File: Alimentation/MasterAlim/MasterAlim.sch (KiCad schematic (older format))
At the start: 51 parts, among them J1 Ext-Con, J10 Interf-Reg1, J11 AU Logic, J12 Interf-Reg2, J13 Interf-Reg3, J14 Interf-Reg4, J2 5V, J3 Bat. IN, J5 Direct Out, J6 Reg 1, J7 Reg 2, J8 Reg 3, J9 Reg 4, U1 74LS33, U3 ACS712xLCTR-20A, U6 PTN78020W_EUK-7, U7 ACS712xLCTR-20A

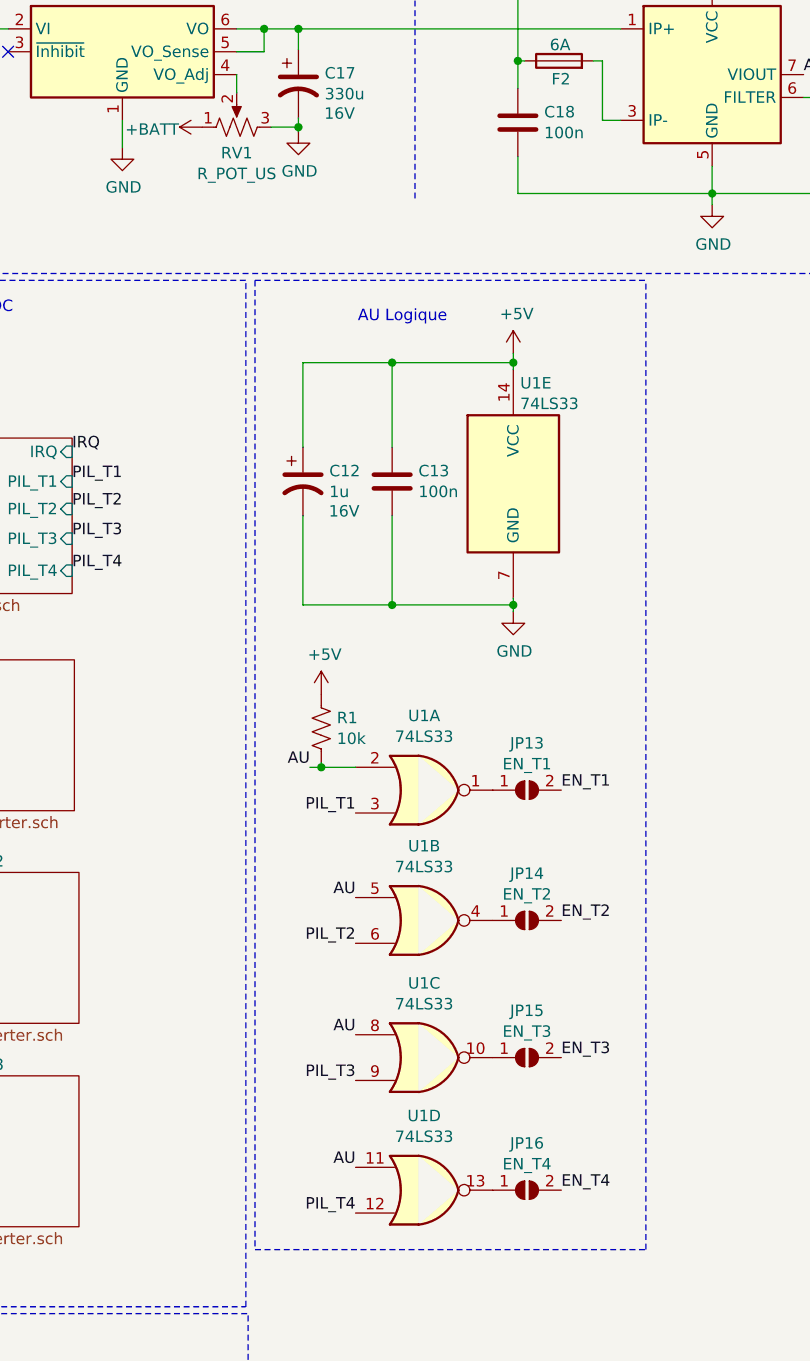
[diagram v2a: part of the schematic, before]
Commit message: Module alimentation 6A
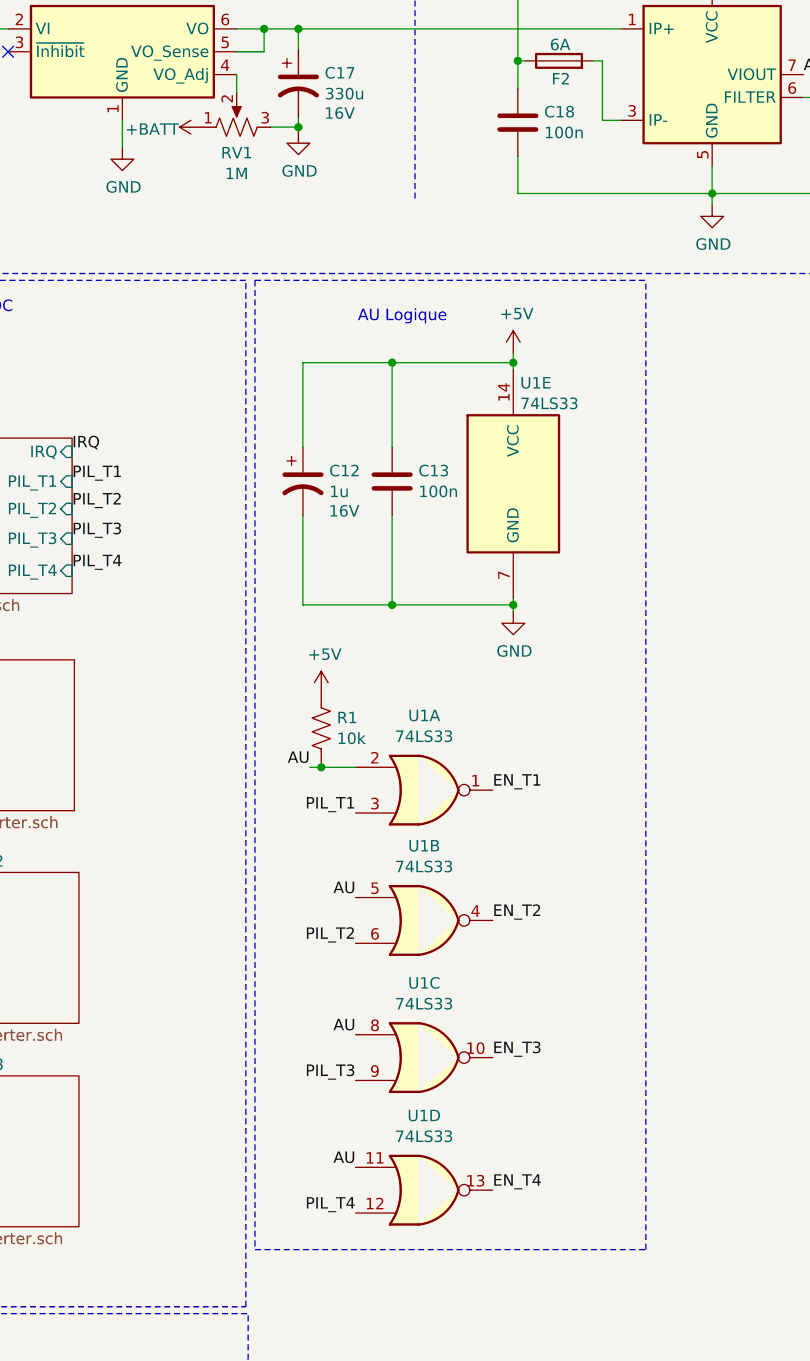
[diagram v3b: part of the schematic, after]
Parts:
- removed JP13: EN_T1, Jumper:SolderJumper-2_P1.3mm_Open_RoundedPad1.0x1.5mm, symbol Jumper:SolderJumper_2_Open
- removed JP14: EN_T2, Jumper:SolderJumper-2_P1.3mm_Open_RoundedPad1.0x1.5mm, symbol Jumper:SolderJumper_2_Open
- removed JP15: EN_T3, Jumper:SolderJumper-2_P1.3mm_Open_RoundedPad1.0x1.5mm, symbol Jumper:SolderJumper_2_Open
- removed JP16: EN_T4, Jumper:SolderJumper-2_P1.3mm_Open_RoundedPad1.0x1.5mm, symbol Jumper:SolderJumper_2_Open
- RV1: value R_POT_US -> 1M
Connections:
- net EN_T1: now also U1.1
- net EN_T2: now also U1.4
- net EN_T3: now also U1.10
- net EN_T4: now also U1.13
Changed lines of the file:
@@
 Text Label 7010 6320 2    50   ~ 0
 PIL_T4
-Text Label 7910 6220 0    50   ~ 0
+Text Label 7610 6220 0    50   ~ 0
 EN_T4
-Text Label 7910 5640 0    50   ~ 0
+Text Label 7610 5640 0    50   ~ 0
 EN_T3
-Text Label 7910 4470 0    50   ~ 0
+Text Label 7610 4470 0    50   ~ 0
 EN_T1
 Wire Notes Line
@@
 Wire Wire Line
 	5770 7010 5770 6990
-Text Label 7910 5040 0    50   ~ 0
+Text Label 7610 5040 0    50   ~ 0
 EN_T2
 $Comp
@@
 P 6490 1570
 F 0 "RV1" V 6377 1570 50  0000 C CNN
-F 1 "R_POT_US" V 6286 1570 50  0000 C CNN
+F 1 "1M" V 6286 1570 50  0000 C CNN
 F 2 "Potentiometer_SMD:Potentiometer_Bourns_TC33X_Vertical" H 6490 1570 50  0001 C CNN
 F 3 "~" H 6490 1570 50  0001 C CNN
@@
 	1    0    0    -1
 $EndComp
-$Comp
-L Jumper:SolderJumper_2_Open JP13
-U 1 1 5FC8DEE2
-P 7760 4470
-F 0 "JP13" H 7760 4675 50  0000 C CNN
-F 1 "EN_T1" H 7760 4584 50  0000 C CNN
-F 2 "Jumper:SolderJumper-2_P1.3mm_Open_RoundedPad1.0x1.5mm" H 7760 4470 50  0001 C CNN
-F 3 "~" H 7760 4470 50  0001 C CNN
-	1    7760 4470
-	1    0    0    -1
-$EndComp
-$Comp
-L Jumper:SolderJumper_2_Open JP14
-U 1 1 5FCA7ABF
-P 7760 5040
-F 0 "JP14" H 7760 5245 50  0000 C CNN
-F 1 "EN_T2" H 7760 5154 50  0000 C CNN
-F 2 "Jumper:SolderJumper-2_P1.3mm_Open_RoundedPad1.0x1.5mm" H 7760 5040 50  0001 C CNN
-F 3 "~" H 7760 5040 50  0001 C CNN
-	1    7760 5040
-	1    0    0    -1
-$EndComp
-$Comp
-L Jumper:SolderJumper_2_Open JP15
-U 1 1 5FCA8A3F
-P 7760 5640
-F 0 "JP15" H 7760 5845 50  0000 C CNN
-F 1 "EN_T3" H 7760 5754 50  0000 C CNN
-F 2 "Jumper:SolderJumper-2_P1.3mm_Open_RoundedPad1.0x1.5mm" H 7760 5640 50  0001 C CNN
-F 3 "~" H 7760 5640 50  0001 C CNN
-	1    7760 5640
-	1    0    0    -1
-$EndComp
-$Comp
-L Jumper:SolderJumper_2_Open JP16
-U 1 1 5FCA9630
-P 7760 6220
-F 0 "JP16" H 7760 6425 50  0000 C CNN
-F 1 "EN_T4" H 7760 6334 50  0000 C CNN
-F 2 "Jumper:SolderJumper-2_P1.3mm_Open_RoundedPad1.0x1.5mm" H 7760 6220 50  0001 C CNN
-F 3 "~" H 7760 6220 50  0001 C CNN
-	1    7760 6220
-	1    0    0    -1
-$EndComp

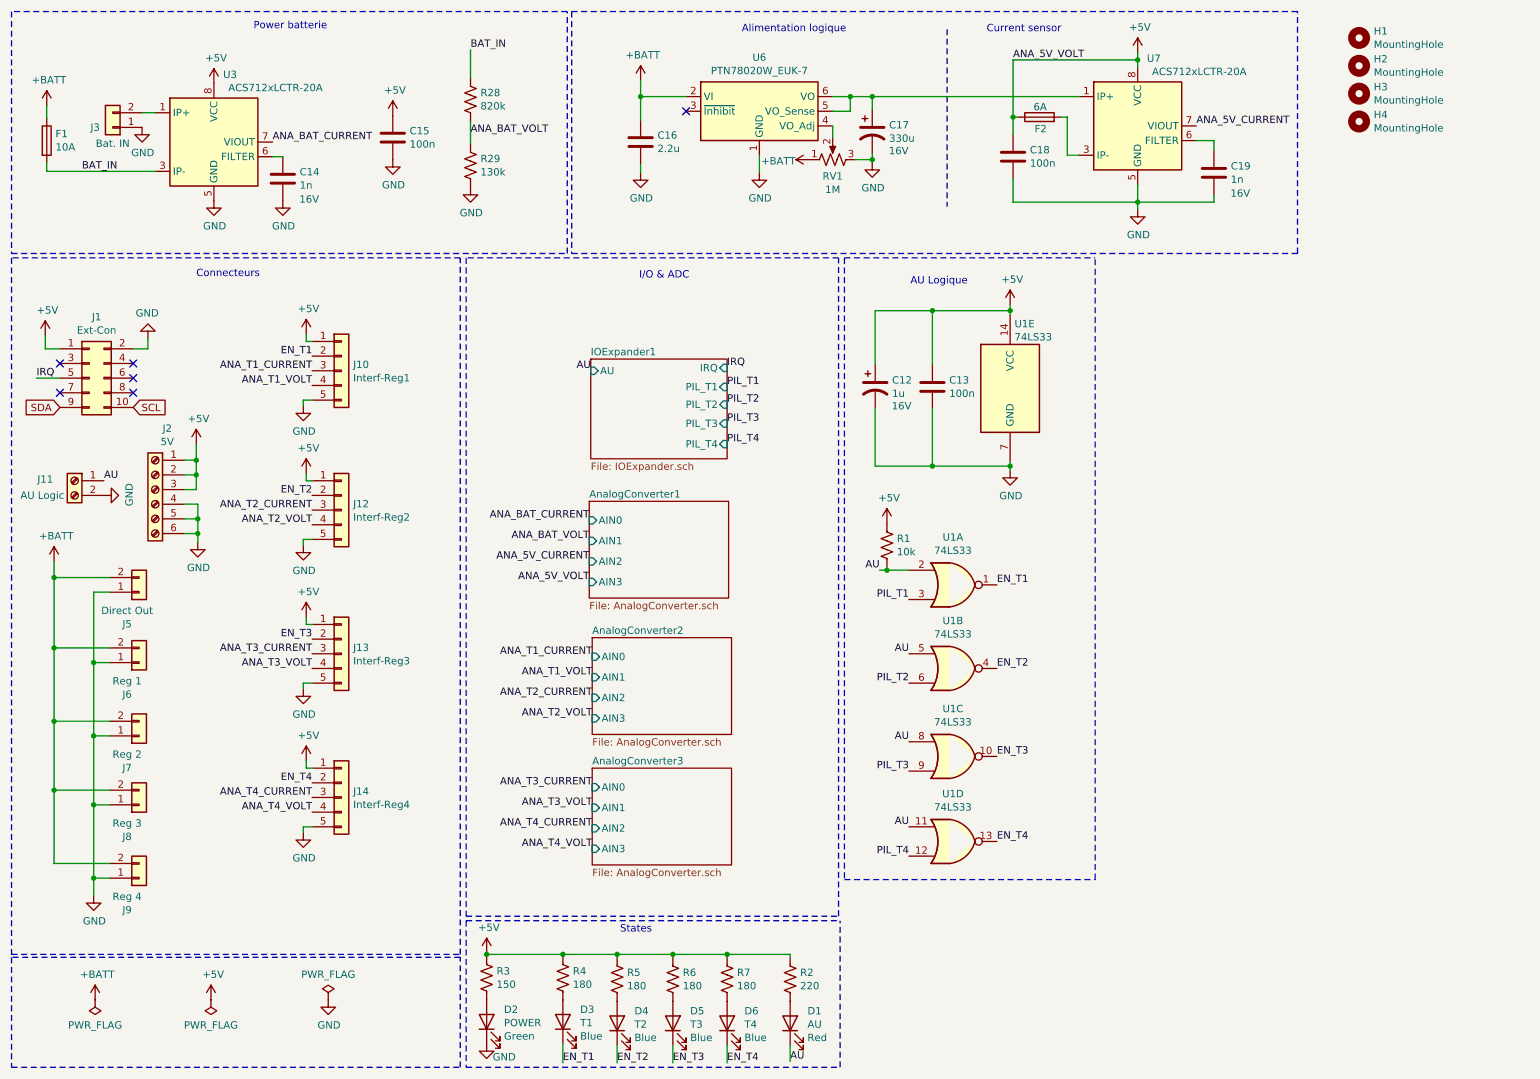
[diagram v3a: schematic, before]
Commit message: Module alim ISO, clean master alim
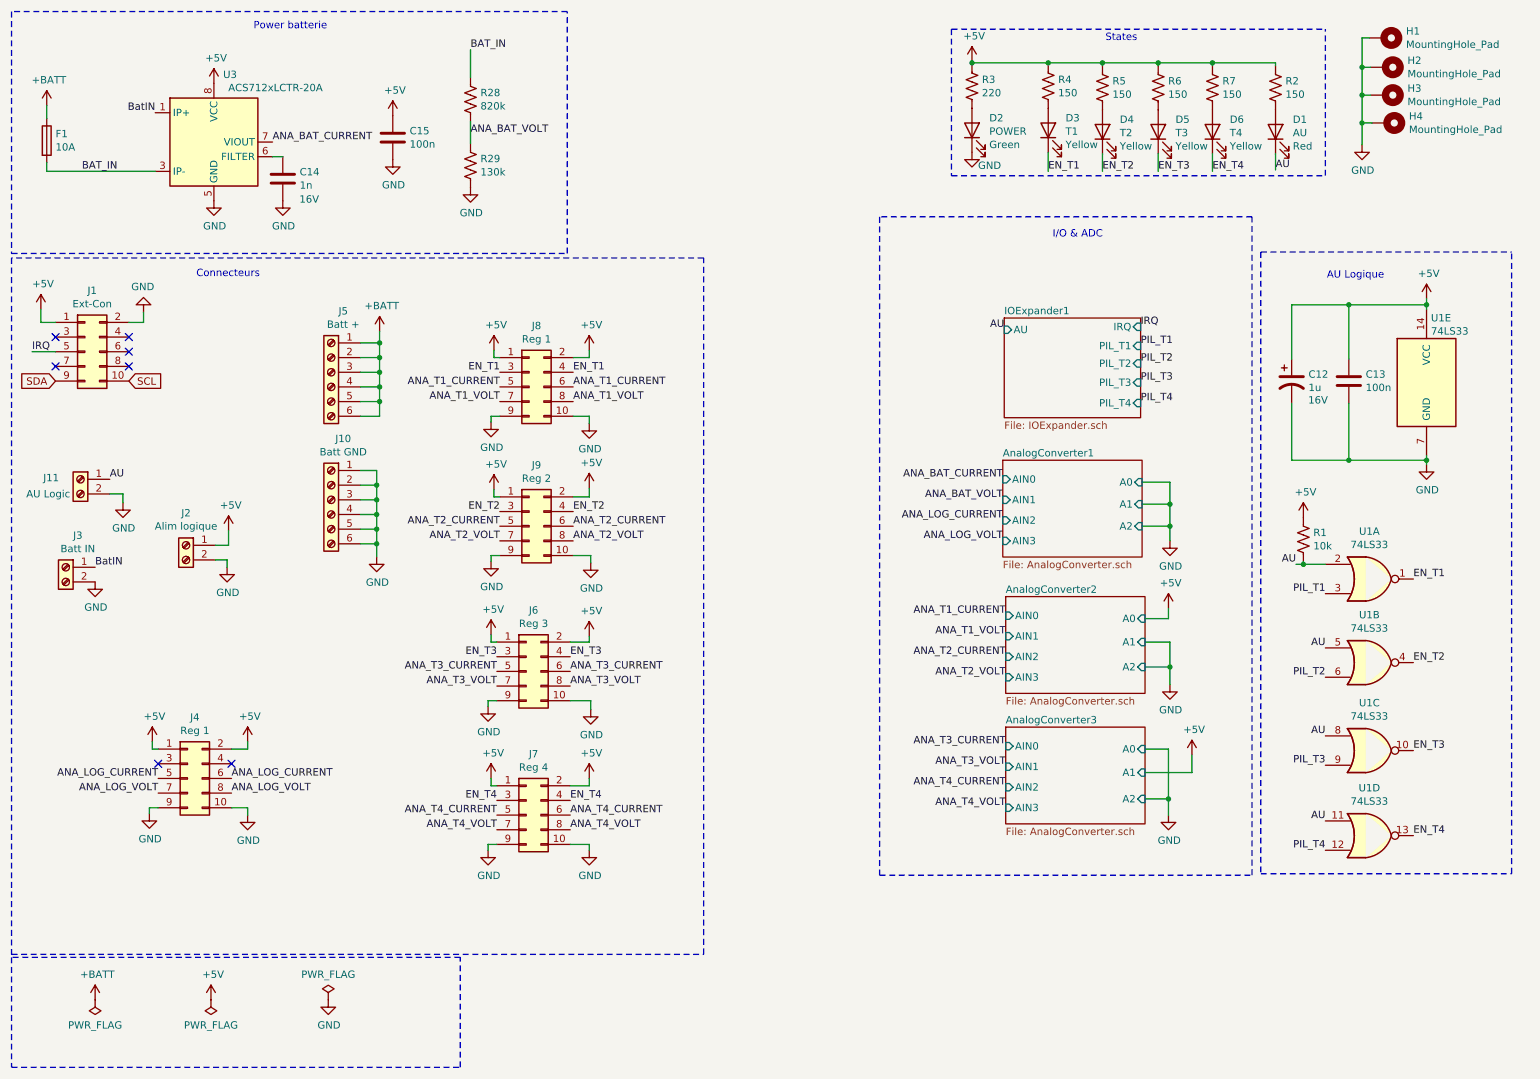
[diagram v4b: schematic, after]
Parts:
- removed C16: 2.2u, Capacitor_SMD:C_0805_2012Metric_Pad1.18x1.45mm_HandSolder, symbol Device:C
- removed C17: 330u, Capacitor_SMD:CP_Elec_10x10, symbol Device:CP1
- removed C18: 100n, Capacitor_SMD:C_0805_2012Metric_Pad1.18x1.45mm_HandSolder, symbol Device:C
- removed C19: 1n, Capacitor_SMD:C_0603_1608Metric_Pad1.08x0.95mm_HandSolder, symbol Device:C
- removed F2: 6A, Fuse:Fuseholder_Cylinder-5x20mm_Schurter_0031_8201_Horizontal_Open, symbol Device:Fuse
- removed H1, H2, H3, H4: MountingHole, MountingHole:MountingHole_3.2mm_M3, symbol Mechanical:MountingHole
- removed J10: Interf-Reg1, Connector_JST:JST_PH_B5B-PH-K_1x05_P2.00mm_Vertical, symbol Connector_Generic:Conn_01x05
- removed J12: Interf-Reg2, Connector_JST:JST_PH_B5B-PH-K_1x05_P2.00mm_Vertical, symbol Connector_Generic:Conn_01x05
- removed J13: Interf-Reg3, Connector_JST:JST_PH_B5B-PH-K_1x05_P2.00mm_Vertical, symbol Connector_Generic:Conn_01x05
- removed J14: Interf-Reg4, Connector_JST:JST_PH_B5B-PH-K_1x05_P2.00mm_Vertical, symbol Connector_Generic:Conn_01x05
- removed J2: 5V, TerminalBlock_Phoenix:TerminalBlock_Phoenix_MPT-0,5-6-2.54_1x06_P2.54mm_Horizontal, symbol Connector:Screw_Terminal_01x06
- removed J3: Bat. IN, Connector_Phoenix_MC_HighVoltage:PhoenixContact_MC_1,5_2-G-5.08_1x02_P5.08mm_Horizontal, symbol Connector_Generic:Conn_01x02
- removed J5: Direct Out, Connector_Phoenix_MC_HighVoltage:PhoenixContact_MC_1,5_2-G-5.08_1x02_P5.08mm_Horizontal, symbol Connector_Generic:Conn_01x02
- removed J6: Reg 1, Connector_Phoenix_MC_HighVoltage:PhoenixContact_MC_1,5_2-G-5.08_1x02_P5.08mm_Horizontal, symbol Connector_Generic:Conn_01x02
- removed J7: Reg 2, Connector_Phoenix_MC_HighVoltage:PhoenixContact_MC_1,5_2-G-5.08_1x02_P5.08mm_Horizontal, symbol Connector_Generic:Conn_01x02
- removed J8: Reg 3, Connector_Phoenix_MC_HighVoltage:PhoenixContact_MC_1,5_2-G-5.08_1x02_P5.08mm_Horizontal, symbol Connector_Generic:Conn_01x02
- removed J9: Reg 4, Connector_Phoenix_MC_HighVoltage:PhoenixContact_MC_1,5_2-G-5.08_1x02_P5.08mm_Horizontal, symbol Connector_Generic:Conn_01x02
- removed RV1: 1M, Potentiometer_SMD:Potentiometer_Bourns_TC33X_Vertical, symbol Device:R_POT_US
- removed U6: PTN78020W_EUK-7, ARIG:Texas_EUK_R-PDSS-T7_THT, symbol ARIG:PTN78020W_EUK-7
- removed U7: ACS712xLCTR-20A, Package_SO:SOIC-8_3.9x4.9mm_P1.27mm, symbol Sensor_Current:ACS712xLCTR-20A
- added H1, H2, H3, H4: MountingHole_Pad, MountingHole:MountingHole_3.2mm_M3_Pad_Via, symbol Mechanical:MountingHole_Pad
- added J10: Batt GND, TerminalBlock_Phoenix:TerminalBlock_Phoenix_MKDS-1,5-6-5.08_1x06_P5.08mm_Horizontal, symbol Connector:Screw_Terminal_01x06
- added J2: Alim logique, TerminalBlock_Phoenix:TerminalBlock_Phoenix_MKDS-1,5-2-5.08_1x02_P5.08mm_Horizontal, symbol Connector:Screw_Terminal_01x02
- added J3: Batt IN, TerminalBlock_Phoenix:TerminalBlock_Phoenix_MKDS-1,5-2-5.08_1x02_P5.08mm_Horizontal, symbol Connector:Screw_Terminal_01x02
- added J4, J8: Reg 1, Connector_IDC:IDC-Header_2x05_P2.54mm_Vertical, symbol Connector_Generic:Conn_02x05_Odd_Even
- added J5: Batt +, TerminalBlock_Phoenix:TerminalBlock_Phoenix_MKDS-1,5-6-5.08_1x06_P5.08mm_Horizontal, symbol Connector:Screw_Terminal_01x06
- added J6: Reg 3, Connector_IDC:IDC-Header_2x05_P2.54mm_Vertical, symbol Connector_Generic:Conn_02x05_Odd_Even
- added J7: Reg 4, Connector_IDC:IDC-Header_2x05_P2.54mm_Vertical, symbol Connector_Generic:Conn_02x05_Odd_Even
- added J9: Reg 2, Connector_IDC:IDC-Header_2x05_P2.54mm_Vertical, symbol Connector_Generic:Conn_02x05_Odd_Even
- C13, C15: footprint Capacitor_SMD:C_0805_2012Metric_Pad1.18x1.45mm_HandSolder -> Capacitor_SMD:C_0603_1608Metric_Pad1.08x0.95mm_HandSolder; LCSC Part C28233 -> C80516; Tension (none) -> 16V
- C14: LCSC C163169 -> (none); LCSC Part (none) -> C163169
- D2: LCSC Part C205442 -> C63855
- D3, D4, D5, D6: Color Blue -> Yellow; LCSC Part C205441 -> C74346
- R2: value 220 -> 150; LCSC Part C417010 -> C17471
- R3: value 150 -> 220; LCSC Part C17471 -> C417010
- R4, R5, R6, R7: value 180 -> 150; LCSC Part C168485 -> C17471
- U1: footprint Package_DIP:DIP-14_W7.62mm_Socket -> Package_DIP:DIP-14_W7.62mm_Socket_LongPads; JLCPCB BOM (none) -> 0
- U1: footprint Package_DIP:DIP-14_W7.62mm_Socket -> Package_DIP:DIP-14_W7.62mm_Socket_LongPads
- U3: LCSC Part (none) -> C10681
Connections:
- net +5V: now also J2.1 (Pin_1), J4.1 (Pin_1), J4.2 (Pin_2), J6.1 (Pin_1), J6.2 (Pin_2), J7.1 (Pin_1), J7.2 (Pin_2), J8.1 (Pin_1), J8.2 (Pin_2), J9.1 (Pin_1), J9.2 (Pin_2)
- net +BATT: now also J5.1 (Pin_1), J5.2 (Pin_2), J5.3 (Pin_3), J5.4 (Pin_4), J5.5 (Pin_5), J5.6 (Pin_6)
- net ANA_T1_CURRENT: now also J8.5 (Pin_5), J8.6 (Pin_6)
- net ANA_T1_VOLT: now also J8.7 (Pin_7), J8.8 (Pin_8)
- net ANA_T2_CURRENT: now also J9.5 (Pin_5), J9.6 (Pin_6)
- net ANA_T2_VOLT: now also J9.7 (Pin_7), J9.8 (Pin_8)
- net ANA_T3_CURRENT: now also J6.5 (Pin_5), J6.6 (Pin_6)
- net ANA_T3_VOLT: now also J6.7 (Pin_7), J6.8 (Pin_8)
- net ANA_T4_CURRENT: now also J7.5 (Pin_5), J7.6 (Pin_6)
- net ANA_T4_VOLT: now also J7.7 (Pin_7), J7.8 (Pin_8)
- net EN_T1: now also J8.3 (Pin_3), J8.4 (Pin_4)
- net EN_T2: now also J9.3 (Pin_3), J9.4 (Pin_4)
- net EN_T3: now also J6.3 (Pin_3), J6.4 (Pin_4)
- net EN_T4: now also J7.3 (Pin_3), J7.4 (Pin_4)
- net GND: now also H1.1, H2.1, H3.1, H4.1, J10.1 (Pin_1), J10.2 (Pin_2), J10.3 (Pin_3), J10.4 (Pin_4), J10.5 (Pin_5), J10.6 (Pin_6), J2.2 (Pin_2), J3.2 (Pin_2), J4.10 (Pin_10), J4.9 (Pin_9), J6.10 (Pin_10), J6.9 (Pin_9), J7.10 (Pin_10), J7.9 (Pin_9), J8.10 (Pin_10), J8.9 (Pin_9), J9.10 (Pin_10), J9.9 (Pin_9)
- net BatIN: now reaches U3.1 (IP+), U3.2 (IP+)
- net BatIN: now also J3.1 (Pin_1)
- new net ANA_LOG_CURRENT: J4.5 (Pin_5), J4.6 (Pin_6)
- new net ANA_LOG_VOLT: J4.7 (Pin_7), J4.8 (Pin_8)
- no-connect marks 6 -> 7
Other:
- note removed: "Alimentation logique"
- note removed: "Current sensor"
- moved on the sheet: C12, C13, D1, D2, D3, D4, D5, D6, J1, J11, R1, R2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
